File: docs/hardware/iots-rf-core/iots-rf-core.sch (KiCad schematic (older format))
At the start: 3 parts, among them U1 MoteinoR6

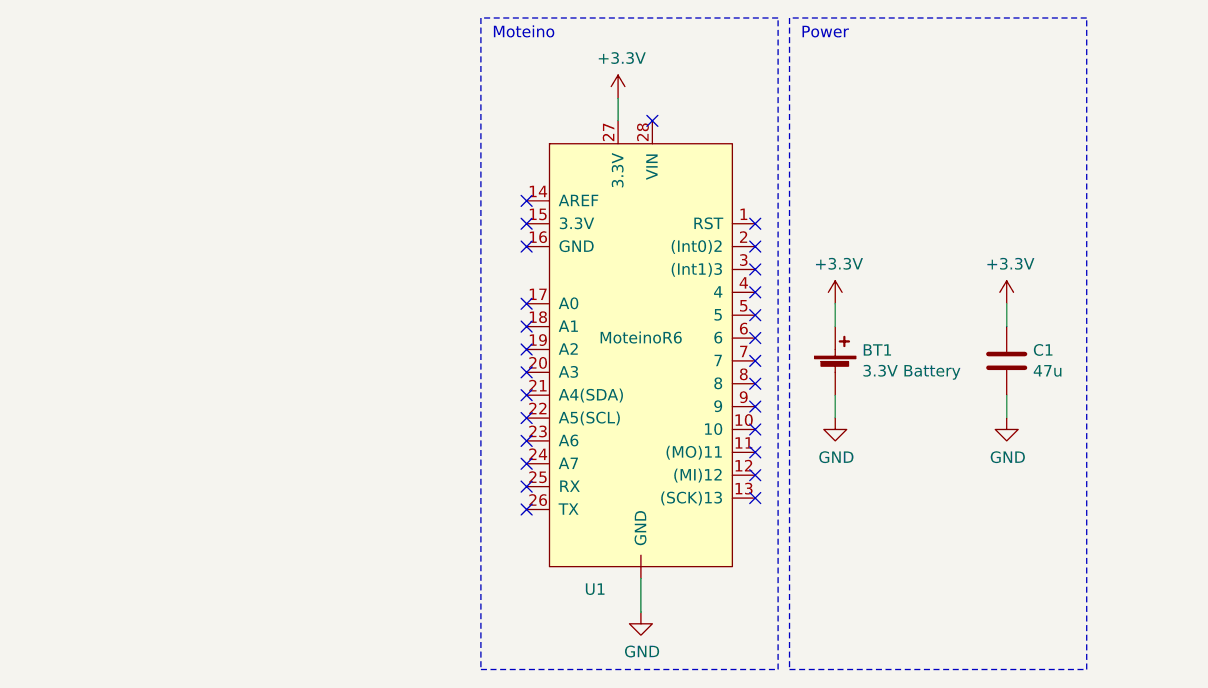
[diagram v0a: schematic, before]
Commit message: Refactor FSM & basic states
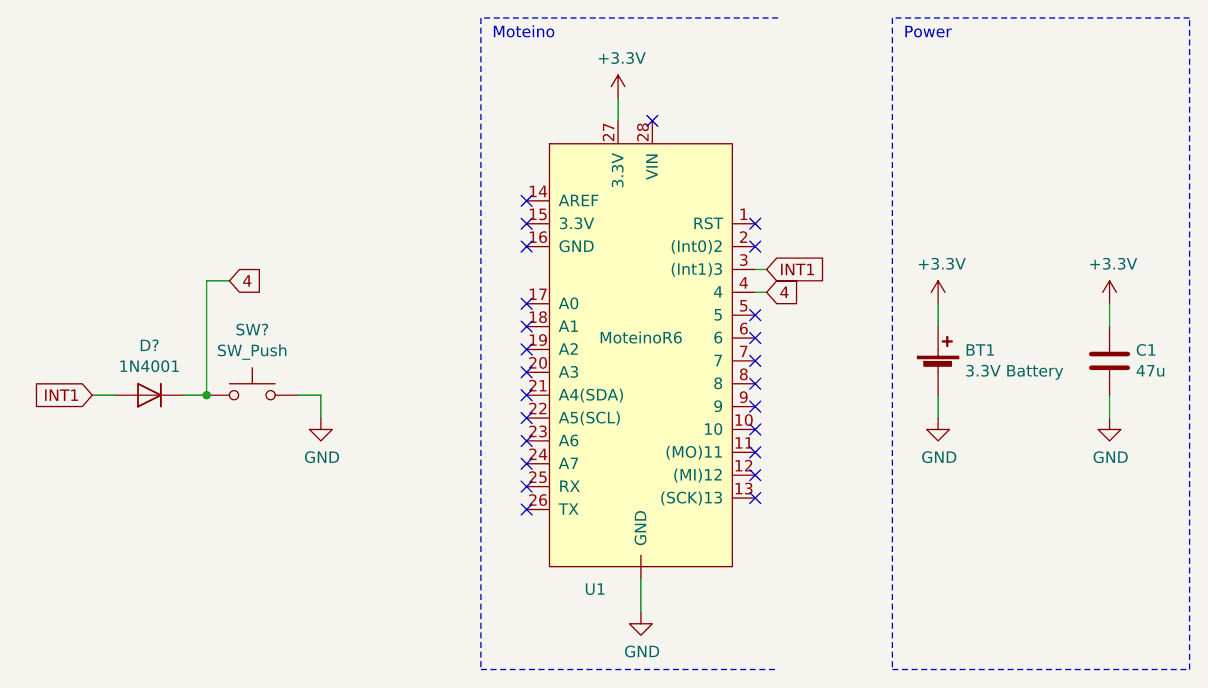
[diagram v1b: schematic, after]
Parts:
- added D?: 1N4001, Diode_THT:D_DO-41_SOD81_P10.16mm_Horizontal, symbol Diode:1N4001
- added SW?: SW_Push, symbol Switch:SW_Push
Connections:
- net GND: now also SW?.2
- net INT1: now reaches U1.3 ((Int1)3)
- net INT1: now also D?.2 (A)
- net 4: now reaches U1.4
- net 4: now also D?.1 (K), SW?.1
- no-connect marks 27 -> 25
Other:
- moved on the sheet: BT1, C1
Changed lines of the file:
@@
 L Device:C C1
 U 1 1 620D7D15
-P 6900 3400
-F 0 "C1" H 7015 3446 50  0000 L CNN
-F 1 "47u" H 7015 3355 50  0000 L CNN
-F 2 "" H 6938 3250 50  0001 C CNN
-F 3 "~" H 6900 3400 50  0001 C CNN
-	1    6900 3400
+P 7350 3400
+F 0 "C1" H 7465 3446 50  0000 L CNN
+F 1 "47u" H 7465 3355 50  0000 L CNN
+F 2 "" H 7388 3250 50  0001 C CNN
+F 3 "~" H 7350 3400 50  0001 C CNN
+	1    7350 3400
 	1    0    0    -1
 $EndComp
@@
 L Device:Battery_Cell BT1
 U 1 1 620D8FEC
-P 6150 3450
-F 0 "BT1" H 6268 3546 50  0000 L CNN
-F 1 "3.3V Battery" H 6268 3455 50  0000 L CNN
-F 2 "" V 6150 3510 50  0001 C CNN
-F 3 "~" V 6150 3510 50  0001 C CNN
-	1    6150 3450
+P 6600 3450
+F 0 "BT1" H 6718 3546 50  0000 L CNN
+F 1 "3.3V Battery" H 6718 3455 50  0000 L CNN
+F 2 "" V 6600 3510 50  0001 C CNN
+F 3 "~" V 6600 3510 50  0001 C CNN
+	1    6600 3450
 	1    0    0    -1
 $EndComp
@@
 L power:+3.3V #PWR03
 U 1 1 620D987E
-P 6150 3150
-F 0 "#PWR03" H 6150 3000 50  0001 C CNN
-F 1 "+3.3V" H 6165 3323 50  0000 C CNN
-F 2 "" H 6150 3150 50  0001 C CNN
-F 3 "" H 6150 3150 50  0001 C CNN
-	1    6150 3150
+P 6600 3150
+F 0 "#PWR03" H 6600 3000 50  0001 C CNN
+F 1 "+3.3V" H 6615 3323 50  0000 C CNN
+F 2 "" H 6600 3150 50  0001 C CNN
+F 3 "" H 6600 3150 50  0001 C CNN
+	1    6600 3150
 	1    0    0    -1
 $EndComp
@@
 L power:GND #PWR04
 U 1 1 620D9B81
-P 6150 3650
-F 0 "#PWR04" H 6150 3400 50  0001 C CNN
-F 1 "GND" H 6155 3477 50  0000 C CNN
-F 2 "" H 6150 3650 50  0001 C CNN
-F 3 "" H 6150 3650 50  0001 C CNN
-	1    6150 3650
+P 6600 3650
+F 0 "#PWR04" H 6600 3400 50  0001 C CNN
+F 1 "GND" H 6605 3477 50  0000 C CNN
+F 2 "" H 6600 3650 50  0001 C CNN
+F 3 "" H 6600 3650 50  0001 C CNN
+	1    6600 3650
 	1    0    0    -1
 $EndComp
@@
 L power:GND #PWR06
 U 1 1 620DB6DB
-P 6900 3650
-F 0 "#PWR06" H 6900 3400 50  0001 C CNN
-F 1 "GND" H 6905 3477 50  0000 C CNN
-F 2 "" H 6900 3650 50  0001 C CNN
-F 3 "" H 6900 3650 50  0001 C CNN
-	1    6900 3650
+P 7350 3650
+F 0 "#PWR06" H 7350 3400 50  0001 C CNN
+F 1 "GND" H 7355 3477 50  0000 C CNN
+F 2 "" H 7350 3650 50  0001 C CNN
+F 3 "" H 7350 3650 50  0001 C CNN
+	1    7350 3650
 	1    0    0    -1
 $EndComp
@@
 L power:+3.3V #PWR05
 U 1 1 620DB899
-P 6900 3150
-F 0 "#PWR05" H 6900 3000 50  0001 C CNN
-F 1 "+3.3V" H 6915 3323 50  0000 C CNN
-F 2 "" H 6900 3150 50  0001 C CNN
-F 3 "" H 6900 3150 50  0001 C CNN
-	1    6900 3150
-	1    0    0    -1
-$EndComp
-Wire Wire Line
-	6150 3150 6150 3250
-Wire Wire Line
-	6150 3550 6150 3650
-Wire Wire Line
-	6900 3150 6900 3250
-Wire Wire Line
-	6900 3550 6900 3650
+P 7350 3150
+F 0 "#PWR05" H 7350 3000 50  0001 C CNN
+F 1 "+3.3V" H 7365 3323 50  0000 C CNN
+F 2 "" H 7350 3150 50  0001 C CNN
+F 3 "" H 7350 3150 50  0001 C CNN
+	1    7350 3150
+	1    0    0    -1
+$EndComp
+Wire Wire Line
+	6600 3150 6600 3250
+Wire Wire Line
+	6600 3550 6600 3650
+Wire Wire Line
+	7350 3150 7350 3250
+Wire Wire Line
+	7350 3550 7350 3650
 NoConn ~ 5350 2350
 NoConn ~ 5800 2800
 NoConn ~ 5800 2900
-NoConn ~ 5800 3000
-NoConn ~ 5800 3100
 NoConn ~ 5800 3200
 NoConn ~ 5800 3300
@@
 	4600 4750 5900 4750
 Wire Notes Line
-	5900 4750 5900 1900
-Wire Notes Line
 	5900 1900 4600 1900
 Wire Notes Line
-	5950 1900 5950 4750
-Wire Notes Line
-	5950 4750 7250 4750
-Wire Notes Line
-	7250 4750 7250 1900
-Wire Notes Line
-	7250 1900 5950 1900
+	6400 1900 6400 4750
+Wire Notes Line
+	6400 4750 7700 4750
+Wire Notes Line
+	7700 4750 7700 1900
+Wire Notes Line
+	7700 1900 6400 1900
 Text Notes 4650 2000 0    50   ~ 0
 Moteino
-Text Notes 6000 2000 0    50   ~ 0
+Text Notes 6450 2000 0    50   ~ 0
 Power
+Text GLabel 5850 3000 2    50   Input ~ 0
+INT1
+Wire Wire Line
+	5850 3000 5800 3000
+Text GLabel 5850 3100 2    50   Input ~ 0
+4
+Wire Wire Line
+	5850 3100 5800 3100
+$Comp
+L Switch:SW_Push SW?
+U 1 1 621DF84D
+P 3600 3550
+F 0 "SW?" H 3600 3835 50  0000 C CNN
+F 1 "SW_Push" H 3600 3744 50  0000 C CNN
+F 2 "" H 3600 3750 50  0001 C CNN
+F 3 "~" H 3600 3750 50  0001 C CNN
+	1    3600 3550
+	1    0    0    -1
+$EndComp
+$Comp
+L power:GND #PWR?
+U 1 1 621DFD02
+P 3900 3650
+F 0 "#PWR?" H 3900 3400 50  0001 C CNN
+F 1 "GND" H 3905 3477 50  0000 C CNN
+F 2 "" H 3900 3650 50  0001 C CNN
+F 3 "" H 3900 3650 50  0001 C CNN
+	1    3900 3650
+	1    0    0    -1
+$EndComp
+Wire Wire Line
+	3800 3550 3900 3550
+Wire Wire Line
+	3900 3550 3900 3650
+$Comp
+L Diode:1N4001 D?
+U 1 1 621FF080
+P 3150 3550
+F 0 "D?" H 3150 3334 50  0000 C CNN
+F 1 "1N4001" H 3150 3425 50  0000 C CNN
+F 2 "Diode_THT:D_DO-41_SOD81_P10.16mm_Horizontal" H 3150 3375 50  0001 C CNN
+F 3 "http://www.vishay.com/docs/88503/1n4001.pdf" H 3150 3550 50  0001 C CNN
+	1    3150 3550
+	-1   0    0    1
+$EndComp
+Wire Wire Line
+	3400 3550 3300 3550
+Text GLabel 3500 3050 2    50   Input ~ 0
+4
+Text GLabel 2900 3550 0    50   Input ~ 0
+INT1
+Wire Wire Line
+	3500 3050 3400 3050
+Wire Wire Line
+	3400 3050 3400 3550
+Connection ~ 3400 3550
+Wire Wire Line
+	3000 3550 2900 3550
 $EndSCHEMATC
